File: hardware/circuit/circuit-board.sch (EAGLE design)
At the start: 5 parts, among them IC1 ISO7220A

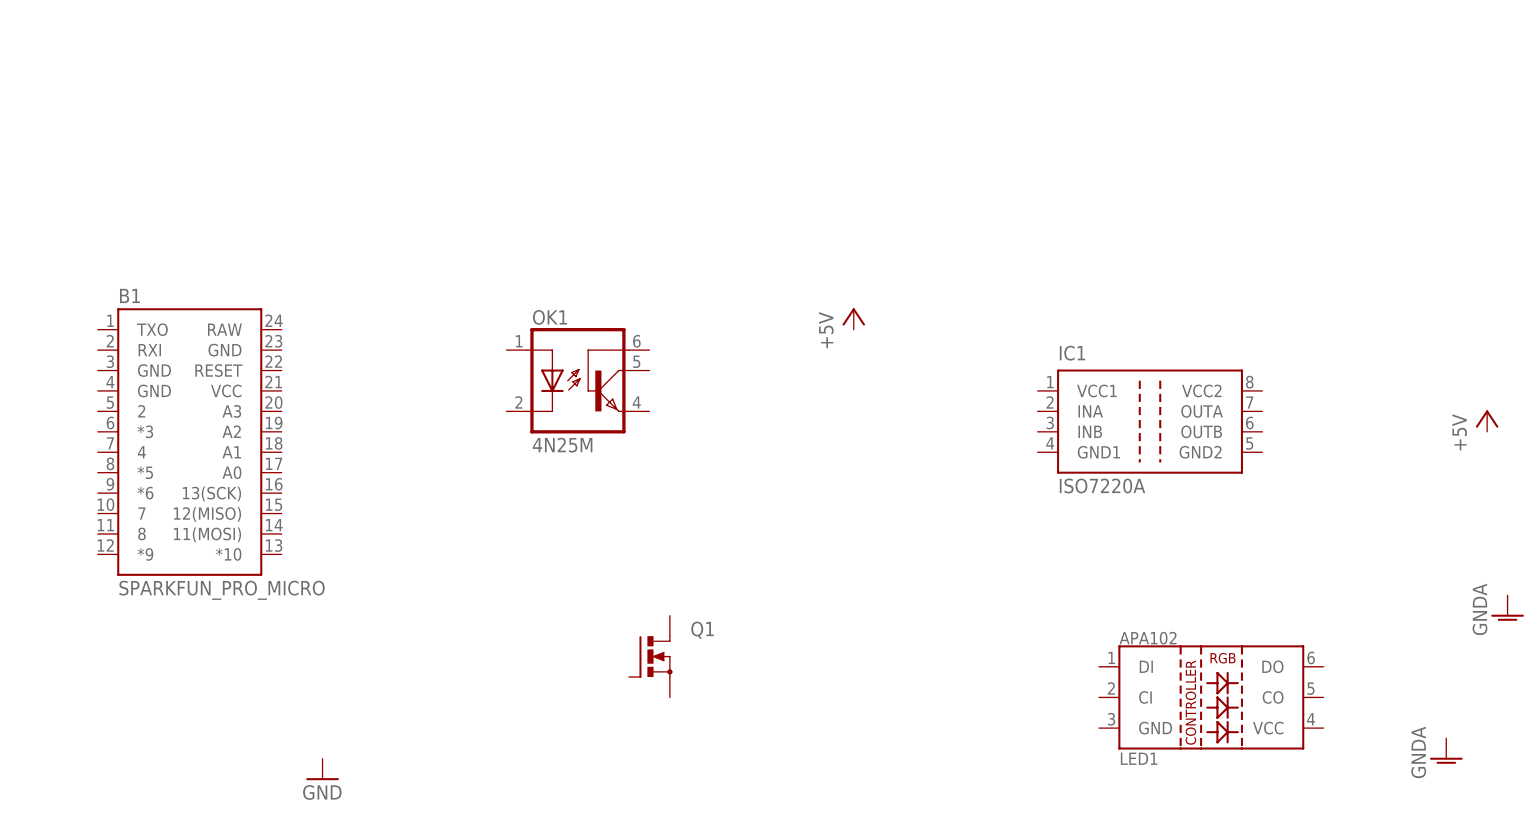
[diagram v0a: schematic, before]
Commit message: Added wiring and some resistor values, replaced ISO7221MDR with ADUM1285CRZ because it has the pin arrangement (both inputs on the same side)
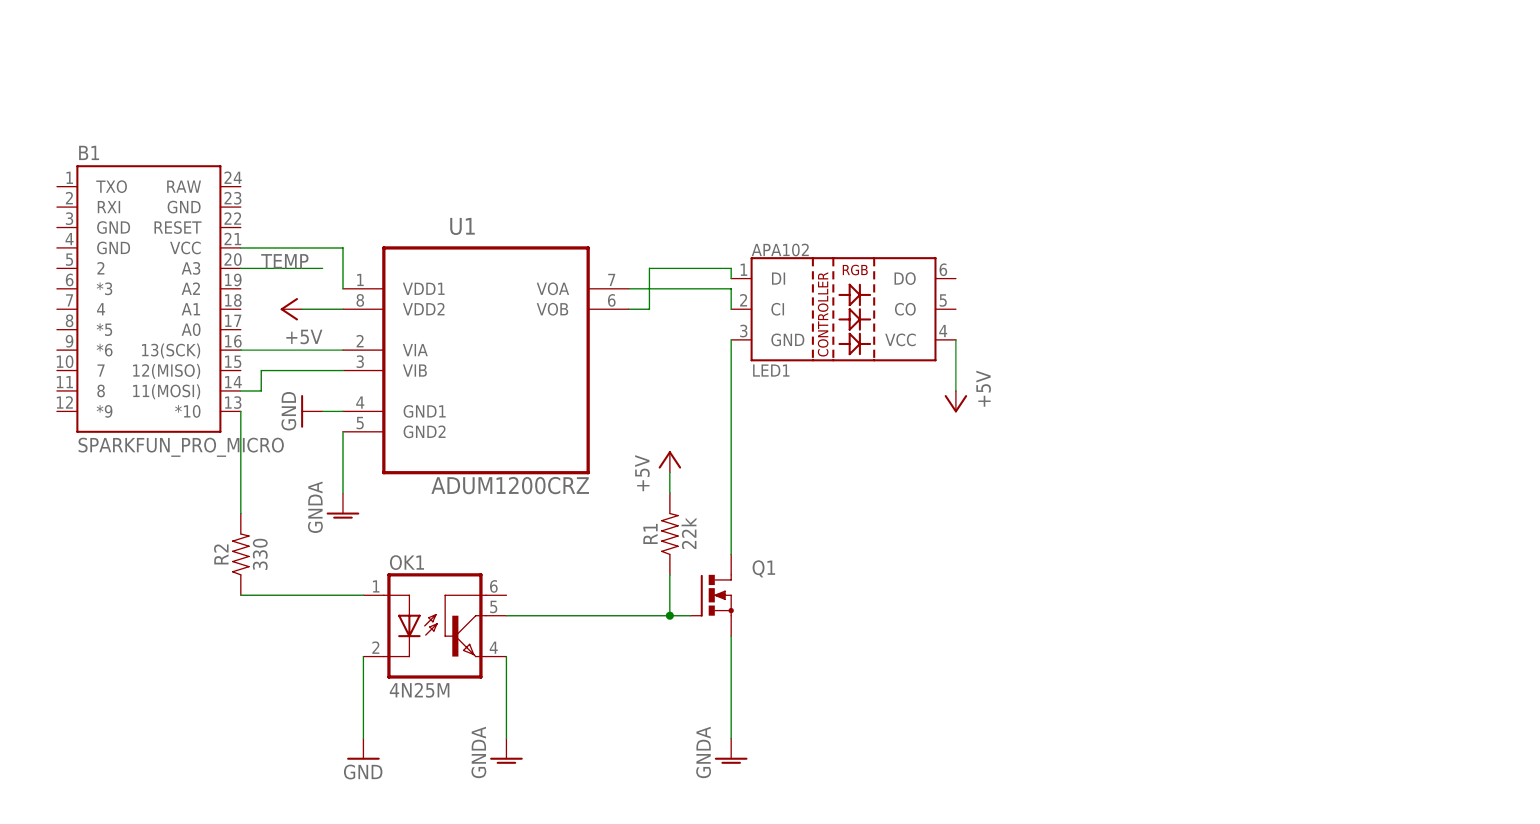
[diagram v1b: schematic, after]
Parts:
- removed IC1: ISO7220A, texas:ISO7220A
- added R1: 22k, SparkFun-Resistors:22KOHM-0603-1/10W-1%
- added R2: 330, SparkFun-Resistors:330OHM-0603-1/10W-1%
- added U1: ADUM1200CRZ, Analog Devices_By_element14_Batch_1:ADUM1200CRZ
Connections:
- new net +5V: LED1.VCC, R1.2, U1.VDD2
- new net GND: OK1.C, U1.GND1
- new net GNDA: OK1.EMI, Q1.S, U1.GND2
- new net N$1: B1.*10, R2.2
- new net N$10: B1.VCC, U1.VDD1
- new net N$2: OK1.COL, Q1.G, R1.1
- new net N$3: LED1.GND, Q1.D
- new net N$4: OK1.A, R2.1
- new net N$5: B1.11(MOSI), U1.VIB
- new net N$6: B1.13(SCK), U1.VIA
- new net N$7: LED1.CI, U1.VOA
- new net N$9: LED1.DI, U1.VOB
- new net TEMP: B1.A3
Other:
- moved on the sheet: B1, LED1, OK1, Q1
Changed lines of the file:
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@@
 <setting verticaltext="up"/>
 </settings>
-<grid distance="0.1" unitdist="inch" unit="inch" style="lines" multiple="1" display="no" altdistance="0.01" altunitdist="inch" altunit="inch"/>
+<grid distance="0.1" unitdist="inch" unit="inch" style="lines" multiple="1" display="yes" altdistance="0.01" altunitdist="inch" altunit="inch"/>
 <layers>
 <layer number="1" name="Top" color="4" fill="11" visible="no" active="no"/>
@@
 <part name="B1" library="SparkFun-Boards" deviceset="SPARKFUN_PRO_MICRO" device=""/>
 <part name="OK1" library="optocoupler" deviceset="4N*?M" device="" technology="25"/>
-<part name="IC1" library="texas" deviceset="ISO7220" device="" technology="A"/>
 <part name="LED1" library="Ai_LED" deviceset="LED-APA102" device=""/>
 <part name="P+1" library="supply1" deviceset="+5V" device=""/>
-<part name="GND1" library="supply1" deviceset="GNDA" device=""/>
 <part name="GND2" library="supply1" deviceset="GND" device=""/>
 <part name="P+2" library="supply1" deviceset="+5V" device=""/>
 <part name="GND3" library="supply1" deviceset="GNDA" device=""/>
+<part name="R2" library="SparkFun-Resistors" deviceset="330OHM" device="-0603-1/10W-1%" value="330"/>
+<part name="R1" library="SparkFun-Resistors" deviceset="22KOHM" device="-0603-1/10W-1%" value="22k"/>
+<part name="GND4" library="supply1" deviceset="GNDA" device=""/>
+<part name="U1" library="Analog Devices_By_element14_Batch_1" deviceset="ADUM1200CRZ" device=""/>
+<part name="GND5" library="supply1" deviceset="GNDA" device=""/>
+<part name="GND6" library="supply1" deviceset="GND" device=""/>
+<part name="P+3" library="supply1" deviceset="+5V" device=""/>
 </parts>
 <sheets>
@@
 </plain>
 <instances>
-<instance part="Q1" gate="G$1" x="55.88" y="50.8"/>
-<instance part="B1" gate="G$1" x="-2.54" y="76.2"/>
-<instance part="OK1" gate="G$1" x="48.26" y="86.36"/>
-<instance part="IC1" gate="G$1" x="116.84" y="78.74"/>
-<instance part="LED1" gate="G$1" x="127" y="45.72"/>
-<instance part="P+1" gate="1" x="160.02" y="81.28"/>
-<instance part="GND1" gate="1" x="162.56" y="55.88"/>
-<instance part="GND2" gate="1" x="15.24" y="35.56"/>
-<instance part="P+2" gate="1" x="81.28" y="93.98"/>
-<instance part="GND3" gate="1" x="154.94" y="38.1"/>
+<instance part="Q1" gate="G$1" x="63.5" y="58.42"/>
+<instance part="B1" gate="G$1" x="-7.62" y="93.98"/>
+<instance part="OK1" gate="G$1" x="30.48" y="55.88"/>
+<instance part="LED1" gate="G$1" x="81.28" y="93.98"/>
+<instance part="P+1" gate="1" x="93.98" y="81.28" rot="R180"/>
+<instance part="GND2" gate="1" x="20.32" y="38.1"/>
+<instance part="P+2" gate="1" x="58.42" y="76.2"/>
+<instance part="GND3" gate="1" x="38.1" y="38.1"/>
+<instance part="R2" gate="G$1" x="5.08" y="63.5" rot="R90"/>
+<instance part="R1" gate="G$1" x="58.42" y="66.04" rot="R90"/>
+<instance part="GND4" gate="1" x="66.04" y="38.1"/>
+<instance part="U1" gate="A" x="35.56" y="91.44"/>
+<instance part="GND5" gate="1" x="17.78" y="68.58"/>
+<instance part="GND6" gate="1" x="12.7" y="81.28" rot="R270"/>
+<instance part="P+3" gate="1" x="10.16" y="93.98" rot="R90"/>
 </instances>
 <busses>
 </busses>
 <nets>
+<net name="GNDA" class="0">
+<segment>
+<pinref part="OK1" gate="G$1" pin="EMI"/>
+<pinref part="GND3" gate="1" pin="GNDA"/>
+<wire x1="38.1" y1="50.8" x2="38.1" y2="40.64" width="0.1524" layer="91"/>
+</segment>
+<segment>
+<pinref part="Q1" gate="G$1" pin="S"/>
+<pinref part="GND4" gate="1" pin="GNDA"/>
+<wire x1="66.04" y1="53.34" x2="66.04" y2="40.64" width="0.1524" layer="91"/>
+</segment>
+<segment>
+<pinref part="U1" gate="A" pin="GND2"/>
+<wire x1="17.78" y1="78.74" x2="17.78" y2="71.12" width="0.1524" layer="91"/>
+<pinref part="GND5" gate="1" pin="GNDA"/>
+</segment>
+</net>
+<net name="+5V" class="0">
+<segment>
+<pinref part="P+2" gate="1" pin="+5V"/>
+<pinref part="R1" gate="G$1" pin="2"/>
+<wire x1="58.42" y1="73.66" x2="58.42" y2="71.12" width="0.1524" layer="91"/>
+</segment>
+<segment>
+<pinref part="P+1" gate="1" pin="+5V"/>
+<pinref part="LED1" gate="G$1" pin="VCC"/>
+<wire x1="93.98" y1="83.82" x2="93.98" y2="90.17" width="0.1524" layer="91"/>
+</segment>
+<segment>
+<pinref part="P+3" gate="1" pin="+5V"/>
+<pinref part="U1" gate="A" pin="VDD2"/>
+<wire x1="12.7" y1="93.98" x2="17.78" y2="93.98" width="0.1524" layer="91"/>
+</segment>
+</net>
+<net name="N$2" class="0">
+<segment>
+<pinref part="R1" gate="G$1" pin="1"/>
+<wire x1="58.42" y1="60.96" x2="58.42" y2="55.88" width="0.1524" layer="91"/>
+<pinref part="OK1" gate="G$1" pin="COL"/>
+<wire x1="58.42" y1="55.88" x2="38.1" y2="55.88" width="0.1524" layer="91"/>
+<wire x1="58.42" y1="55.88" x2="60.96" y2="55.88" width="0.1524" layer="91"/>
+<junction x="58.42" y="55.88"/>
+<pinref part="Q1" gate="G$1" pin="G"/>
+</segment>
+</net>
+<net name="N$3" class="0">
+<segment>
+<pinref part="Q1" gate="G$1" pin="D"/>
+<pinref part="LED1" gate="G$1" pin="GND"/>
+<wire x1="66.04" y1="63.5" x2="66.04" y2="90.17" width="0.1524" layer="91"/>
+</segment>
+</net>
+<net name="GND" class="0">
+<segment>
+<pinref part="GND2" gate="1" pin="GND"/>
+<wire x1="20.32" y1="40.64" x2="20.32" y2="50.8" width="0.1524" layer="91"/>
+<pinref part="OK1" gate="G$1" pin="C"/>
+</segment>
+<segment>
+<pinref part="U1" gate="A" pin="GND1"/>
+<pinref part="GND6" gate="1" pin="GND"/>
+<wire x1="17.78" y1="81.28" x2="15.24" y2="81.28" width="0.1524" layer="91"/>
+</segment>
+</net>
+<net name="N$1" class="0">
+<segment>
+<pinref part="B1" gate="G$1" pin="*10"/>
+<pinref part="R2" gate="G$1" pin="2"/>
+<wire x1="5.08" y1="81.28" x2="5.08" y2="68.58" width="0.1524" layer="91"/>
+</segment>
+</net>
+<net name="N$4" class="0">
+<segment>
+<pinref part="R2" gate="G$1" pin="1"/>
+<pinref part="OK1" gate="G$1" pin="A"/>
+<wire x1="5.08" y1="58.42" x2="20.32" y2="58.42" width="0.1524" layer="91"/>
+</segment>
+</net>
+<net name="N$6" class="0">
+<segment>
+<pinref part="B1" gate="G$1" pin="13(SCK)"/>
+<pinref part="U1" gate="A" pin="VIA"/>
+<wire x1="5.08" y1="88.9" x2="17.78" y2="88.9" width="0.1524" layer="91"/>
+</segment>
+</net>
+<net name="N$7" class="0">
+<segment>
+<pinref part="U1" gate="A" pin="VOA"/>
+<pinref part="LED1" gate="G$1" pin="CI"/>
+<wire x1="53.34" y1="96.52" x2="66.04" y2="96.52" width="0.1524" layer="91"/>
+<wire x1="66.04" y1="96.52" x2="66.04" y2="93.98" width="0.1524" layer="91"/>
+</segment>
+</net>
+<net name="N$9" class="0">
+<segment>
+<pinref part="U1" gate="A" pin="VOB"/>
+<wire x1="53.34" y1="93.98" x2="55.88" y2="93.98" width="0.1524" layer="91"/>
+<wire x1="55.88" y1="93.98" x2="55.88" y2="99.06" width="0.1524" layer="91"/>
+<pinref part="LED1" gate="G$1" pin="DI"/>
+<wire x1="55.88" y1="99.06" x2="66.04" y2="99.06" width="0.1524" layer="91"/>
+<wire x1="66.04" y1="99.06" x2="66.04" y2="97.79" width="0.1524" layer="91"/>
+</segment>
+</net>
+<net name="N$10" class="0">
+<segment>
+<pinref part="B1" gate="G$1" pin="VCC"/>
+<pinref part="U1" gate="A" pin="VDD1"/>
+<wire x1="5.08" y1="101.6" x2="17.78" y2="101.6" width="0.1524" layer="91"/>
+<wire x1="17.78" y1="101.6" x2="17.78" y2="96.52" width="0.1524" layer="91"/>
+</segment>
+</net>
+<net name="TEMP" class="0">
+<segment>
+<pinref part="B1" gate="G$1" pin="A3"/>
+<wire x1="5.08" y1="99.06" x2="15.24" y2="99.06" width="0.1524" layer="91"/>
+<label x="7.62" y="99.06" size="1.778" layer="95"/>
+</segment>
+</net>
+<net name="N$5" class="0">
+<segment>
+<pinref part="B1" gate="G$1" pin="11(MOSI)"/>
+<wire x1="5.08" y1="83.82" x2="7.62" y2="83.82" width="0.1524" layer="91"/>
+<wire x1="7.62" y1="83.82" x2="7.62" y2="86.36" width="0.1524" layer="91"/>
+<pinref part="U1" gate="A" pin="VIB"/>
+<wire x1="7.62" y1="86.36" x2="17.78" y2="86.36" width="0.1524" layer="91"/>
+</segment>
+</net>
 </nets>
 </sheet>

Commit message: Added temperature sensor to circuit schematic
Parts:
- added R3: 1k, SparkFun-Resistors:1KOHM-0603-1/10W-1%
- added U$1: LM335AZ, pmandal:LM335AZ
- R2: value 330 -> 1k; device SparkFun-Resistors:330OHM-0603-1/10W-1% -> SparkFun-Resistors:1KOHM-0603-1/10W-1%
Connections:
- net GND: now also U$1.A
- net N$10: now also R3.2
- net TEMP: now also R3.1, U$1.C
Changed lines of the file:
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@@
 <part name="P+2" library="supply1" deviceset="+5V" device=""/>
 <part name="GND3" library="supply1" deviceset="GNDA" device=""/>
-<part name="R2" library="SparkFun-Resistors" deviceset="330OHM" device="-0603-1/10W-1%" value="330"/>
 <part name="R1" library="SparkFun-Resistors" deviceset="22KOHM" device="-0603-1/10W-1%" value="22k"/>
 <part name="GND4" library="supply1" deviceset="GNDA" device=""/>
@@
 <part name="GND6" library="supply1" deviceset="GND" device=""/>
 <part name="P+3" library="supply1" deviceset="+5V" device=""/>
+<part name="R2" library="SparkFun-Resistors" deviceset="1KOHM" device="-0603-1/10W-1%" value="1k"/>
+<part name="U$1" library="pmandal" deviceset="LM335AZ" device=""/>
+<part name="GND1" library="supply1" deviceset="GND" device=""/>
+<part name="R3" library="SparkFun-Resistors" deviceset="1KOHM" device="-0603-1/10W-1%" value="1k"/>
 </parts>
 <sheets>
@@
 <instance part="P+2" gate="1" x="58.42" y="76.2"/>
 <instance part="GND3" gate="1" x="38.1" y="38.1"/>
-<instance part="R2" gate="G$1" x="5.08" y="63.5" rot="R90"/>
 <instance part="R1" gate="G$1" x="58.42" y="66.04" rot="R90"/>
 <instance part="GND4" gate="1" x="66.04" y="38.1"/>
@@
 <instance part="GND6" gate="1" x="12.7" y="81.28" rot="R270"/>
 <instance part="P+3" gate="1" x="10.16" y="93.98" rot="R90"/>
+<instance part="R2" gate="G$1" x="5.08" y="63.5" rot="R90"/>
+<instance part="U$1" gate="G$1" x="17.78" y="119.38" rot="R270"/>
+<instance part="GND1" gate="1" x="17.78" y="127" rot="R180"/>
+<instance part="R3" gate="G$1" x="17.78" y="106.68" rot="R270"/>
 </instances>
 <busses>
@@
 <wire x1="17.78" y1="81.28" x2="15.24" y2="81.28" width="0.1524" layer="91"/>
 </segment>
+<segment>
+<pinref part="U$1" gate="G$1" pin="A"/>
+<pinref part="GND1" gate="1" pin="GND"/>
+<wire x1="17.78" y1="121.92" x2="17.78" y2="124.46" width="0.1524" layer="91"/>
+</segment>
 </net>
 <net name="N$1" class="0">
 <segment>
 <pinref part="B1" gate="G$1" pin="*10"/>
+<wire x1="5.08" y1="81.28" x2="5.08" y2="68.58" width="0.1524" layer="91"/>
 <pinref part="R2" gate="G$1" pin="2"/>
-<wire x1="5.08" y1="81.28" x2="5.08" y2="68.58" width="0.1524" layer="91"/>
 </segment>
 </net>
 <net name="N$4" class="0">
 <segment>
-<pinref part="R2" gate="G$1" pin="1"/>
 <pinref part="OK1" gate="G$1" pin="A"/>
 <wire x1="5.08" y1="58.42" x2="20.32" y2="58.42" width="0.1524" layer="91"/>
+<pinref part="R2" gate="G$1" pin="1"/>
 </segment>
 </net>
@@
 <wire x1="5.08" y1="101.6" x2="17.78" y2="101.6" width="0.1524" layer="91"/>
 <wire x1="17.78" y1="101.6" x2="17.78" y2="96.52" width="0.1524" layer="91"/>
+<pinref part="R3" gate="G$1" pin="2"/>
+<junction x="17.78" y="101.6"/>
 </segment>
 </net>
@@
 <label x="7.62" y="99.06" size="1.778" layer="95"/>
 </segment>
+<segment>
+<pinref part="R3" gate="G$1" pin="1"/>
+<pinref part="U$1" gate="G$1" pin="C"/>
+<wire x1="17.78" y1="111.76" x2="17.78" y2="114.3" width="0.1524" layer="91"/>
+<wire x1="17.78" y1="114.3" x2="17.78" y2="116.84" width="0.1524" layer="91"/>
+<wire x1="17.78" y1="114.3" x2="30.48" y2="114.3" width="0.1524" layer="91"/>
+<junction x="17.78" y="114.3"/>
+<label x="22.86" y="114.3" size="1.778" layer="95"/>
+</segment>
 </net>

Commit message: Rerouted wiring for 4N25 optocoupler - signal was being inverted
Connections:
- removed net N$1: B1.*10, R2.2
- removed net N$10: B1.VCC, R3.2, U1.VDD1
- new net N$8: B1.*10, OK1.C
- new net VCC: B1.VCC, R2.2, R3.2, U1.VDD1
- net GND: no longer OK1.C
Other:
- moved on the sheet: R2
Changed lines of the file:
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@@
 <setting verticaltext="up"/>
 </settings>
-<grid distance="0.1" unitdist="inch" unit="inch" style="lines" multiple="1" display="yes" altdistance="0.01" altunitdist="inch" altunit="inch"/>
+<grid distance="0.1" unitdist="inch" unit="inch" style="lines" multiple="1" display="no" altdistance="0.01" altunitdist="inch" altunit="inch"/>
 <layers>
 <layer number="1" name="Top" color="4" fill="11" visible="no" active="no"/>
@@
 <part name="LED1" library="Ai_LED" deviceset="LED-APA102" device=""/>
 <part name="P+1" library="supply1" deviceset="+5V" device=""/>
-<part name="GND2" library="supply1" deviceset="GND" device=""/>
 <part name="P+2" library="supply1" deviceset="+5V" device=""/>
 <part name="GND3" library="supply1" deviceset="GNDA" device=""/>
@@
 <instance part="LED1" gate="G$1" x="81.28" y="93.98"/>
 <instance part="P+1" gate="1" x="93.98" y="81.28" rot="R180"/>
-<instance part="GND2" gate="1" x="20.32" y="38.1"/>
 <instance part="P+2" gate="1" x="58.42" y="76.2"/>
 <instance part="GND3" gate="1" x="38.1" y="38.1"/>
@@
 <instance part="GND6" gate="1" x="12.7" y="81.28" rot="R270"/>
 <instance part="P+3" gate="1" x="10.16" y="93.98" rot="R90"/>
-<instance part="R2" gate="G$1" x="5.08" y="63.5" rot="R90"/>
+<instance part="R2" gate="G$1" x="7.62" y="58.42" rot="R180"/>
 <instance part="U$1" gate="G$1" x="17.78" y="119.38" rot="R270"/>
 <instance part="GND1" gate="1" x="17.78" y="127" rot="R180"/>
@@
 <net name="GND" class="0">
 <segment>
-<pinref part="GND2" gate="1" pin="GND"/>
-<wire x1="20.32" y1="40.64" x2="20.32" y2="50.8" width="0.1524" layer="91"/>
-<pinref part="OK1" gate="G$1" pin="C"/>
-</segment>
-<segment>
 <pinref part="U1" gate="A" pin="GND1"/>
 <pinref part="GND6" gate="1" pin="GND"/>
@@
 <pinref part="GND1" gate="1" pin="GND"/>
 <wire x1="17.78" y1="121.92" x2="17.78" y2="124.46" width="0.1524" layer="91"/>
-</segment>
-</net>
-<net name="N$1" class="0">
-<segment>
-<pinref part="B1" gate="G$1" pin="*10"/>
-<wire x1="5.08" y1="81.28" x2="5.08" y2="68.58" width="0.1524" layer="91"/>
-<pinref part="R2" gate="G$1" pin="2"/>
-</segment>
-</net>
-<net name="N$4" class="0">
-<segment>
-<pinref part="OK1" gate="G$1" pin="A"/>
-<wire x1="5.08" y1="58.42" x2="20.32" y2="58.42" width="0.1524" layer="91"/>
-<pinref part="R2" gate="G$1" pin="1"/>
 </segment>
 </net>
@@
 </segment>
 </net>
-<net name="N$10" class="0">
+<net name="VCC" class="0">
 <segment>
 <pinref part="B1" gate="G$1" pin="VCC"/>
@@
 <pinref part="R3" gate="G$1" pin="2"/>
 <junction x="17.78" y="101.6"/>
+</segment>
+<segment>
+<pinref part="R2" gate="G$1" pin="2"/>
+<wire x1="2.54" y1="58.42" x2="-7.62" y2="58.42" width="0.1524" layer="91"/>
+<label x="-2.54" y="60.96" size="1.778" layer="95" rot="R180"/>
 </segment>
 </net>
@@
 </segment>
 </net>
+<net name="N$4" class="0">
+<segment>
+<pinref part="R2" gate="G$1" pin="1"/>
+<pinref part="OK1" gate="G$1" pin="A"/>
+<wire x1="12.7" y1="58.42" x2="20.32" y2="58.42" width="0.1524" layer="91"/>
+</segment>
+</net>
+<net name="N$8" class="0">
+<segment>
+<pinref part="OK1" gate="G$1" pin="C"/>
+<wire x1="20.32" y1="50.8" x2="-22.86" y2="50.8" width="0.1524" layer="91"/>
+<wire x1="-22.86" y1="50.8" x2="-22.86" y2="68.58" width="0.1524" layer="91"/>
+<wire x1="-22.86" y1="68.58" x2="5.08" y2="68.58" width="0.1524" layer="91"/>
+<pinref part="B1" gate="G$1" pin="*10"/>
+<wire x1="5.08" y1="68.58" x2="5.08" y2="81.28" width="0.1524" layer="91"/>
+</segment>
+</net>
